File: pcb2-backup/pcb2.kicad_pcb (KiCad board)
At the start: 2 copper layers, 100 x 102.4 mm, 72 parts, among them J1 WQP419GR_audio_in_1, J10 ACJS-HHOP_pedal_3, J11 ACJS-HHOP_pedal_4, J12 PMOD_JD, J13 PMOD_JC, J14 ACJS-HHOP_audio_out_L, J15 ACJS-HHOP_audio_out_R, J2 WQP419GR_audio_in_3, J3 Barrel_+5V_in, J4 Conn_+5V_to_FPGA, J5 Conn_GND_to_FPGA, J6 WQP419GR_audio_in_2, J7 WQP419GR_audio_in_4, J8 ACJS-HHOP_pedal_1, J9 ACJS-HHOP_pedal_2, U1 LM3940, U2 PCM1840, U3 ADC104S021, U4 TAD5242

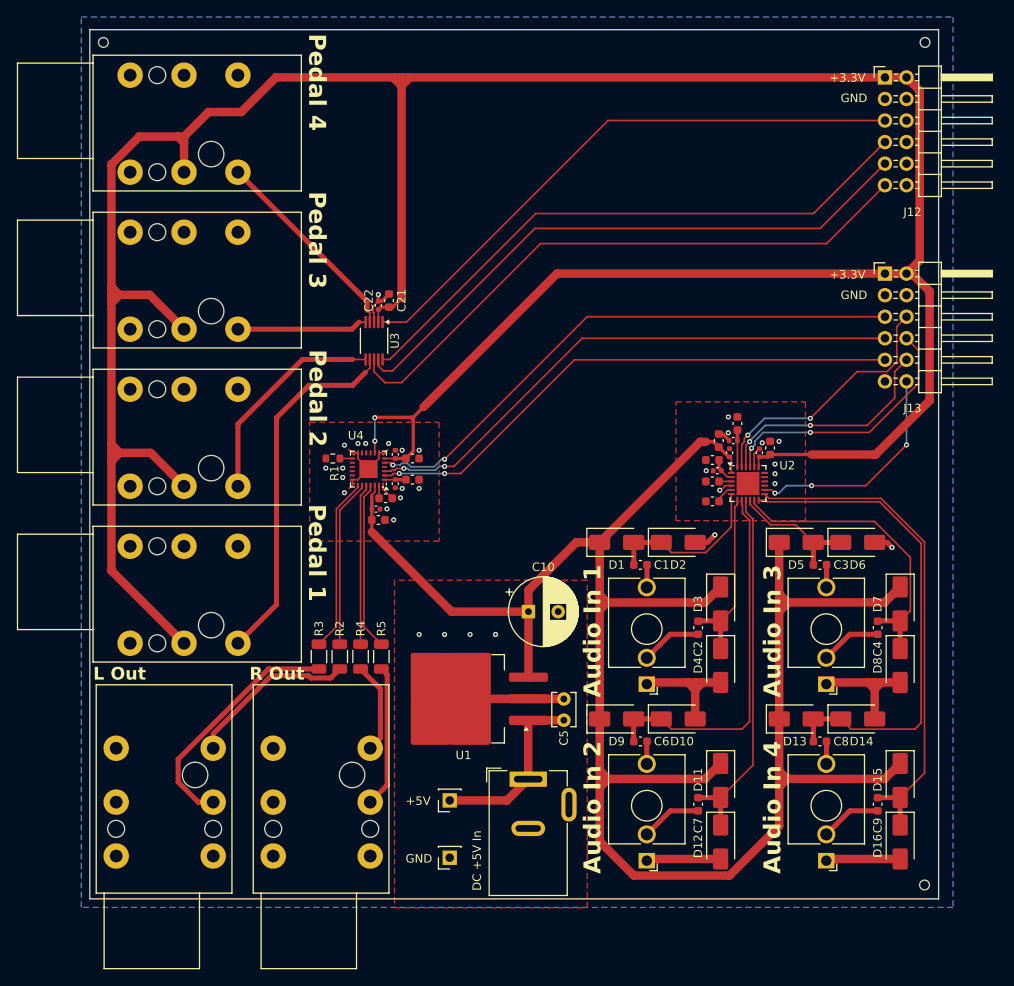
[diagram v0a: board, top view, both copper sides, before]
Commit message: Implement expression pedal controls
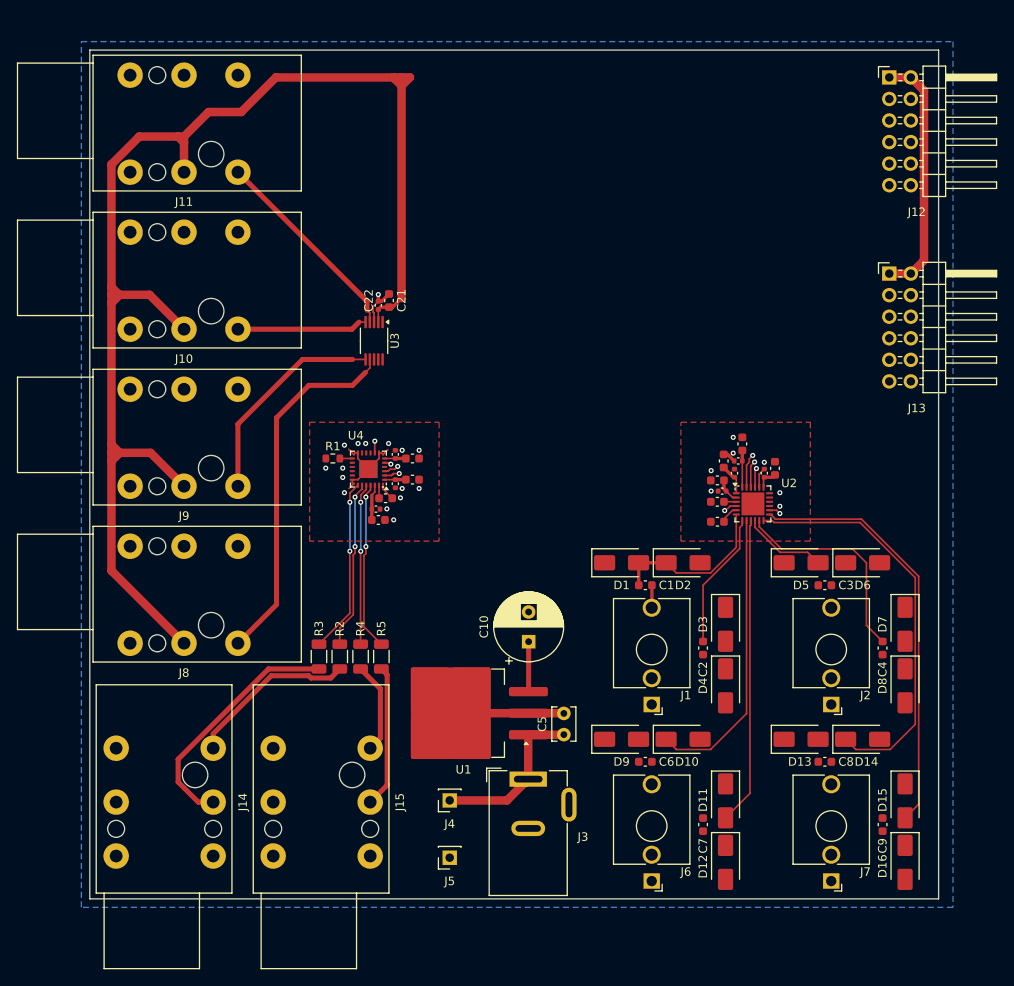
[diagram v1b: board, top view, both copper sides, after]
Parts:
- removed ToolingHole_JLCPCB_BR, ToolingHole_JLCPCB_TL, ToolingHole_JLCPCB_TR: ToolingHole_JLCPCB, 0_MountingHole:ToolingHole_JLCPCB
- moved C10 3.54 mm to (158.3, 105.8), turned to 90 degrees
- moved C1 2.47 mm to (172.1, 99.2)
- moved C11 2.47 mm to (181.3, 84.6)
- moved C12 2.47 mm to (182.6, 86.0)
- moved C16 2.47 mm to (180.5, 89.4)
- moved C18 2.47 mm to (186.1, 86.0)
- moved C19 2.47 mm to (183.5, 82.5)
- moved C20 2.47 mm to (183.0, 84.6)
- moved C6 2.47 mm to (172.1, 120.0)
- moved C9 2.47 mm to (200.0, 127.4)
- moved D12 2.47 mm to (181.5, 131.8)
- moved D16 2.47 mm to (202.7, 131.8)
- moved J1 2.47 mm to (172.8, 113.2)
- moved J6 2.47 mm to (172.8, 134.1)
- moved C13 2.47 mm to (180.5, 91.7)
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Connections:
- J12 pad 11: /ADC_PEDAL_DIN -> /DAC_DIN
- J12 pad 5: /ADC_PEDAL_CS -> unconnected-(J12-Pin_5-Pad5)
- J12 pad 7: /ADC_PEDAL_CLK -> /DAC_FSYNC
- J12 pad 9: /ADC_PEDAL_DOUT -> /DAC_CLK
- J13 pad 10: /ADC_AUDIO_CLK -> /ADC_AUDIO_DOUT
- J13 pad 11: unconnected-(J13-Pin_11-Pad11) -> /ADC_PEDAL_CS
- J13 pad 5: /DAC_DIN -> /ADC_PEDAL_CLK
- J13 pad 7: /DAC_FSYNC -> /ADC_PEDAL_DOUT
- J13 pad 8: /ADC_AUDIO_DOUT -> /ADC_AUDIO_CLK
- J13 pad 9: /DAC_CLK -> /ADC_PEDAL_DIN
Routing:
- net +3.3VA: track 237.4 -> 13.9 mm
- net +3.3V: track 369.3 -> 200.0 mm, vias 2 -> 1
- net /ADC_PEDAL_DIN: track 71.8 -> 0.00 mm
- net /ADC_PEDAL_DOUT: track 70.8 -> 0.00 mm
- net /ADC_PEDAL_CLK: track 69.8 -> 0.00 mm
- net /ADC_PEDAL_CS: track 69.0 -> 0.00 mm
- net /DAC_DIN: track 66.6 -> 0.81 mm, vias 2 -> 1
- net /DAC_FSYNC: track 65.6 -> 1.79 mm, vias 2 -> 1
- net /DAC_CLK: track 64.6 -> 1.82 mm, vias 2 -> 1
- net GND: track 90.5 -> 37.1 mm, vias 31 -> 24
- net /ADC_AUDIO_DOUT: track 31.2 -> 2.27 mm, vias 2 -> 1
- net /ADC_AUDIO_FSYNC: track 31.0 -> 4.04 mm, vias 2 -> 1
- net /ADC_AUDIO_SHDNZ: track 26.7 -> 1.37 mm, vias 3 -> 1
- net /ADC_AUDIO_CLK: track 27.5 -> 3.16 mm, vias 2 -> 1
- net /ADC_IN4P: track 58.6 -> 47.9 mm
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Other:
- board size 100 x 102.4 mm -> 100 x 100 mm
- board text removed: "+3.3V"
- board text removed: "+5V"
- board text removed: "Audio In 1"
- board text removed: "Audio In 2"
- board text removed: "Audio In 3"
- board text removed: "Audio In 4"
- board text removed: "DC +5V In"
- board text removed: "GND"
- board text removed: "L Out"
- board text removed: "Pedal 1"
- board text removed: "Pedal 2"
- board text removed: "Pedal 3"
- board text removed: "Pedal 4"
- board text removed: "R Out"
